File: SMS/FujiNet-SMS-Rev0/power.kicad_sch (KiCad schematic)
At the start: 15 parts, among them Q2 AO3401A, U12 AP63203WU, U13 AP2112K-3.3

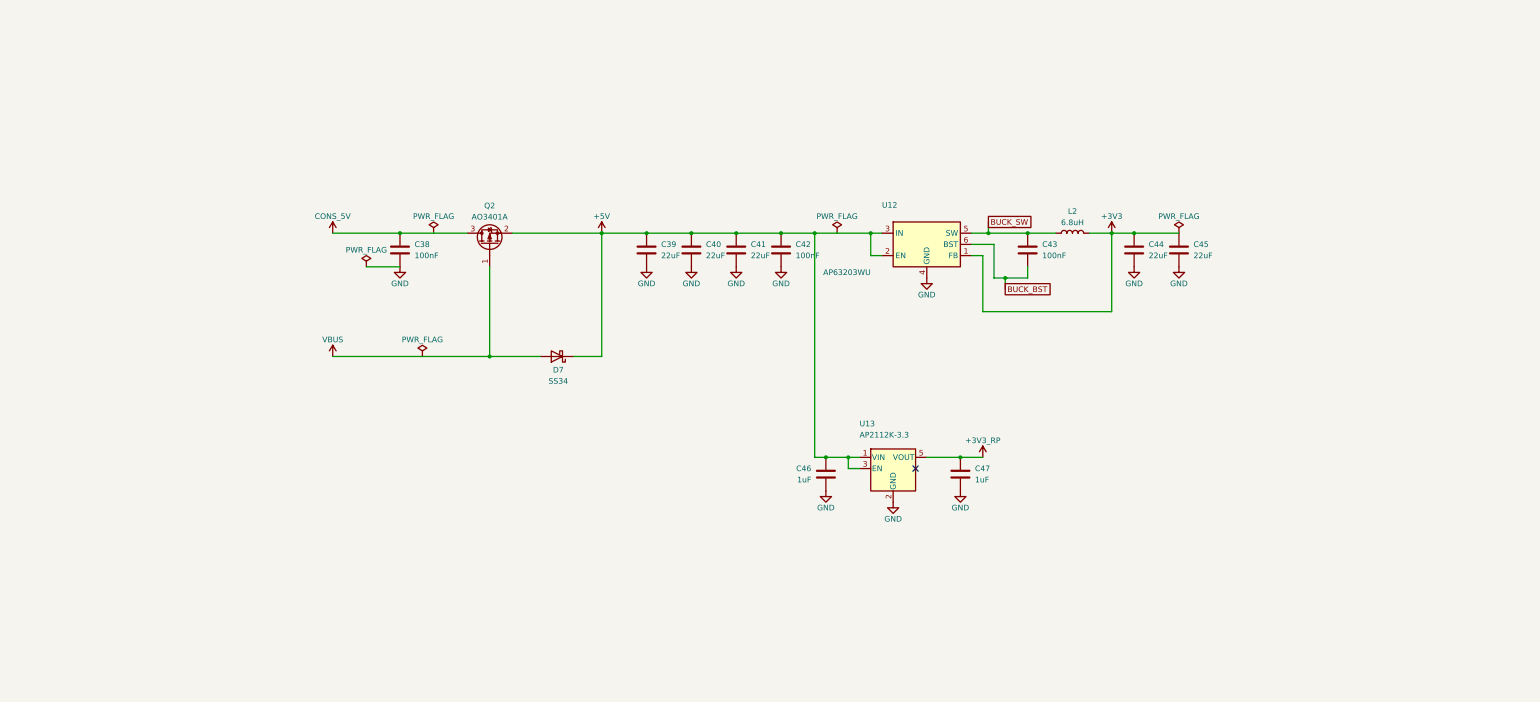
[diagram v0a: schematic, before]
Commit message: SMS Rev0: audit with kicad-happy + datasheets, fix the edge, redraw the schematic
Edge connector: every source (SMS Power slot diagram, little-scale, a 171-5519
scan, raphnet, the barbeque and reidrac footprints) puts the EVEN pins on the
component / label side with pins 1/2 at the right.  The schematic-only
footprint had the faces swapped, which would have put console +5V on /WR.
make_edge_fp.py now writes even pads on F.Cu, odd on B.Cu, 1.75 x 8.75 mm
fingers 0.75-9.5 mm from the edge on a 65.8 mm tab; check_nets.py asserts it
and tools/audit/edge_orientation.py checks it against the sources.

kicad-happy + datasheet audit (docs/design-review-rev0.md Part 1, 27 deep
review findings, gate 27/27): R_VBPD 4.7k VBUS pull-down (SS34 leakage lifts
the P-FET gate), /WAIT gate pull-up 10k -> 4.7k (GPIO34's reset pull-down vs
the 2N7002's 2.5 V threshold), 10 uF bulk on the console 5V.

Schematic: hierarchical sheets wired on a root block diagram (edge -> RP2354B
-> ESP32-S3 -> USB, glue and SRAM under the RP, power below); every sheet
drawn left to right, the glue as a wired logic network by gate depth, the
RP2354B mirrored so its bus faces the console, small sheets on A4.  Parts
are addressed by key (design.py), no more NES reference aliasing.  sch_draw
gains hierarchical labels, sheet blocks, a bus graph and flag / power-pin
lints; gen_sch checks the hierarchy against design.py and names nets by
their last path element (one bus vector per bus: KiCad joins differing
vectors by position).  ERC 0, check_nets 437/437, check_glue 8192/8192.

JLC CPL rotations measured against the EasyEDA footprint of every LCSC part
(tools/audit/jlc); the AS6C4008 has no EasyEDA footprint.

Co-Authored-By: Claude Opus 5.5 <noreply@anthropic.com>
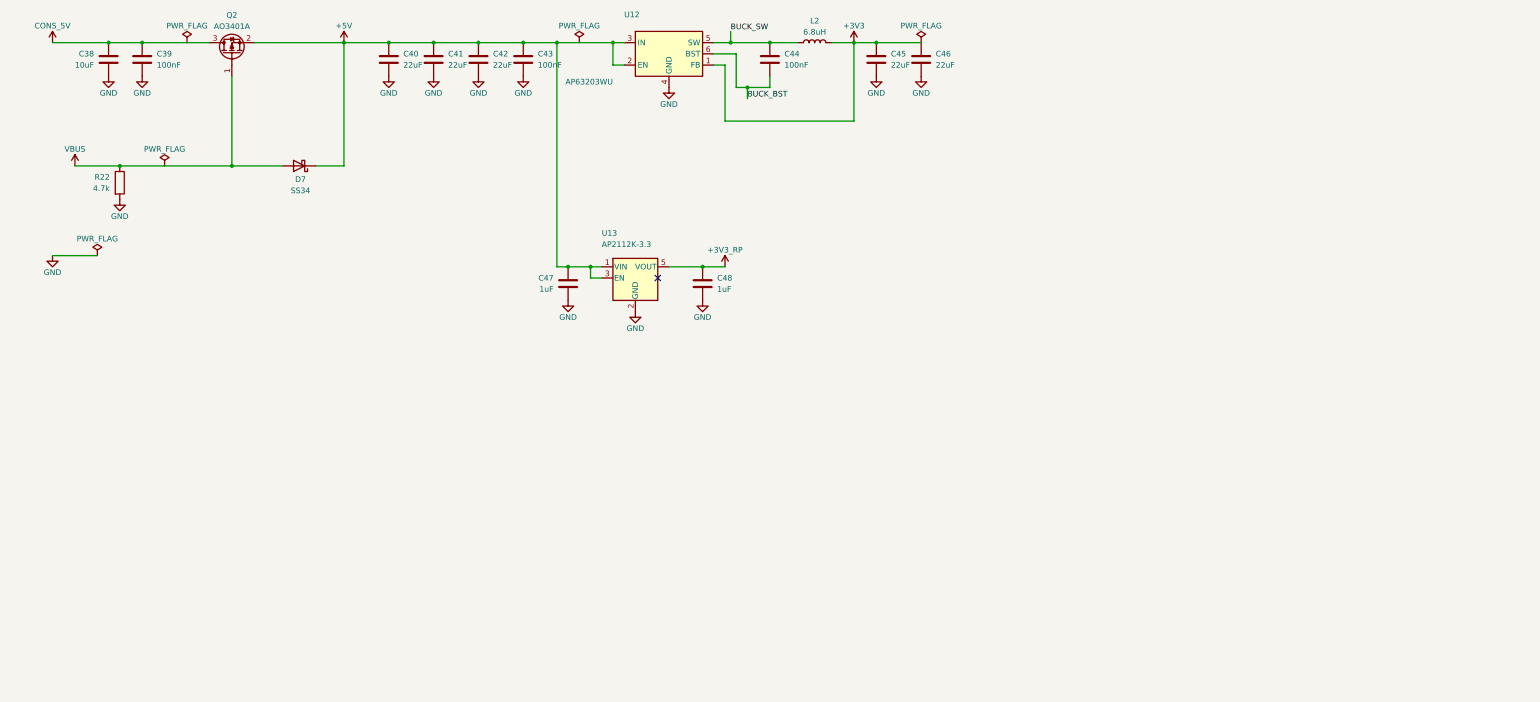
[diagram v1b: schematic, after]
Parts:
- added C48: 1uF, FujiNet-SMS:C_0603_1608Metric, symbol Device:C
- added R22: 4.7k, FujiNet-SMS:R_0603_1608Metric, symbol Device:R
- C38: value 100nF -> 10uF; LCSC C14663 -> C19702; MPN CC0603KRX7R9BB104 -> CL10A106KP8NNNC
- C39, C44: value 22uF -> 100nF; footprint FujiNet-SMS:C_0805_2012Metric -> FujiNet-SMS:C_0603_1608Metric; LCSC C45783 -> C14663; MPN CL21A226MAQNNNE -> CC0603KRX7R9BB104
- C42: value 100nF -> 22uF; footprint FujiNet-SMS:C_0603_1608Metric -> FujiNet-SMS:C_0805_2012Metric; LCSC C14663 -> C45783; MPN CC0603KRX7R9BB104 -> CL21A226MAQNNNE
- C46: value 1uF -> 22uF; footprint FujiNet-SMS:C_0603_1608Metric -> FujiNet-SMS:C_0805_2012Metric; LCSC C15849 -> C45783; MPN CL10A105KB8NNNC -> CL21A226MAQNNNE
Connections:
- net +3V3: now also C46.1; no longer C44.1
- net +3V3_RP: now also C48.1; no longer C47.1
- net +5V: now also C43.1, C47.1; no longer C39.1, C46.1
- net BUCK_BST: now also C44.2; no longer C43.2
- net BUCK_SW: now also C44.1; no longer C43.1
- net CONS_5V: now also C39.1
- net GND: now also C43.2, C48.2, R22.2; no longer C44.2
- net VBUS: now also R22.1
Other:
- moved on the sheet: C38, C39, C40, C41, C42, C43, C44, C45, C46, C47, D7, L2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

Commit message: SMS Rev0 v2: port the FujiNet-7800 tooling, swap the near-stock-out parts
- export.py: JLCPCB and PCBWay packages (PCBWay turnkey BOM, centroid,
  assembly drawing); Manufacturer on every BOM part (design.MFR), written
  to symbols and footprints alike
- edge_geom.py: the SMS edge constants in one place (make_edge_fp,
  gen_pcb, check_gerbers); gen_pcb's body height, holes and In4 split now
  come from placement.py
- footprint paths from the schematic netlist (gen_pcb.fp_sheet_unit), so
  a part's units can be drawn on several sheets (prototype 2026-10-08:
  kicad-cli files it under the first sheet, parity accepts it)
- check_vias, check_gerbers, make_happy_config, stitch_gnd second ring,
  set_models main(), route_board.sh 12 passes / hybrid, DRC at all
  severities
- TL3342 -> TS-1187A-B-A-B (C318884), WS2812B-2020-V6 -> WS2812C-2020-V1
  (C2976072): ~5 in stock on 2026-10-07

Co-Authored-By: Claude Opus 5.5 <noreply@anthropic.com>
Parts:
- C38, C40, C41, C42, C45, C46, C47, C48: Manufacturer (none) -> Samsung Electro-Mechanics
- C39, C43, C44: Manufacturer (none) -> YAGEO
- D7: Manufacturer (none) -> MDD (Microdiode Semiconductor)
- L2: Manufacturer (none) -> Sunlord
- Q2: Manufacturer (none) -> Alpha & Omega Semiconductor
- R22: Manufacturer (none) -> UNI-ROYAL
- U12, U13: Manufacturer (none) -> Diodes Incorporated
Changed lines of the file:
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@@
+			)
+		)
+		(property "Manufacturer" "Alpha & Omega Semiconductor"
+			(at 88.9 63.5 90)
+			(effects
+				(font
+					(size 1.27 1.27)
+				)
+				(hide yes)
 			)
 		)
@@
 			)
 		)
+		(property "Manufacturer" "Samsung Electro-Mechanics"
+			(at 60.96 64.77 0)
+			(effects
+				(font
+					(size 1.27 1.27)
+				)
+				(hide yes)
+			)
+		)
 		(property "LCSC" "C19702"
 			(at 60.96 64.77 0)
@@
 			)
 		)
+		(property "Manufacturer" "YAGEO"
+			(at 68.58 64.77 0)
+			(effects
+				(font
+					(size 1.27 1.27)
+				)
+				(hide yes)
+			)
+		)
 		(property "LCSC" "C14663"
 			(at 68.58 64.77 0)
@@
 			)
 		)
+		(property "Manufacturer" "MDD (Microdiode Semiconductor)"
+			(at 104.14 88.9 0)
+			(effects
+				(font
+					(size 1.27 1.27)
+				)
+				(hide yes)
+			)
+		)
 		(property "LCSC" "C8678"
 			(at 104.14 88.9 0)
@@
 			)
 		)
+		(property "Manufacturer" "UNI-ROYAL"
+			(at 63.5 92.71 0)
+			(effects
+				(font
+					(size 1.27 1.27)
+				)
+				(hide yes)
+			)
+		)
 		(property "LCSC" "C23162"
 			(at 63.5 92.71 0)
@@
 			)
 		)
+		(property "Manufacturer" "Samsung Electro-Mechanics"
+			(at 124.46 64.77 0)
+			(effects
+				(font
+					(size 1.27 1.27)
+				)
+				(hide yes)
+			)
+		)
 		(property "LCSC" "C45783"
 			(at 124.46 64.77 0)
@@
 			)
 		)
+		(property "Manufacturer" "Samsung Electro-Mechanics"
+			(at 134.62 64.77 0)
+			(effects
+				(font
+					(size 1.27 1.27)
+				)
+				(hide yes)
+			)
+		)
 		(property "LCSC" "C45783"
 			(at 134.62 64.77 0)
@@
 			)
 		)
+		(property "Manufacturer" "Samsung Electro-Mechanics"
+			(at 144.78 64.77 0)
+			(effects
+				(font
+					(size 1.27 1.27)
+				)
+				(hide yes)
+			)
+		)
 		(property "LCSC" "C45783"
 			(at 144.78 64.77 0)
@@
 			)
 		)
+		(property "Manufacturer" "YAGEO"
+			(at 154.94 64.77 0)
+			(effects
+				(font
+					(size 1.27 1.27)
+				)
+				(hide yes)
+			)
+		)
 		(property "LCSC" "C14663"
 			(at 154.94 64.77 0)
@@
 			)
 		)
+		(property "Manufacturer" "Diodes Incorporated"
+			(at 187.96 63.5 0)
+			(effects
+				(font
+					(size 1.27 1.27)
+				)
+				(hide yes)
+			)
+		)
 		(property "LCSC" "C780769"
 			(at 187.96 63.5 0)
@@
 			)
 		)
+		(property "Manufacturer" "YAGEO"
+			(at 210.82 64.77 0)
+			(effects
+				(font
+					(size 1.27 1.27)
+				)
+				(hide yes)
+			)
+		)
 		(property "LCSC" "C14663"
 			(at 210.82 64.77 0)
@@
 			)
 		)
+		(property "Manufacturer" "Sunlord"
+			(at 220.98 60.96 90)
+			(effects
+				(font
+					(size 1.27 1.27)
+				)
+				(hide yes)
+			)
+		)
 		(property "LCSC" "C62684"
 			(at 220.98 60.96 90)
@@
 			)
 		)
+		(property "Manufacturer" "Samsung Electro-Mechanics"
+			(at 234.95 64.77 0)
+			(effects
+				(font
+					(size 1.27 1.27)
+				)
+				(hide yes)
+			)
+		)
 		(property "LCSC" "C45783"
 			(at 234.95 64.77 0)
@@
 			)
 		)
+		(property "Manufacturer" "Samsung Electro-Mechanics"
+			(at 245.11 64.77 0)
+			(effects
+				(font
+					(size 1.27 1.27)
+				)
+				(hide yes)
+			)
+		)
 		(property "LCSC" "C45783"
 			(at 245.11 64.77 0)
@@
 			)
 		)
+		(property "Manufacturer" "Diodes Incorporated"
+			(at 180.34 114.3 0)
+			(effects
+				(font
+					(size 1.27 1.27)
+				)
+				(hide yes)
+			)
+		)
 		(property "LCSC" "C51118"
 			(at 180.34 114.3 0)
@@
 			)
 		)
+		(property "Manufacturer" "Samsung Electro-Mechanics"
+			(at 165.1 115.57 0)
+			(effects
+				(font
+					(size 1.27 1.27)
+				)
+				(hide yes)
+			)
+		)
 		(property "LCSC" "C15849"
 			(at 165.1 115.57 0)
@@
 			(at 195.58 115.57 0)
 			(effects
+				(font
+					(size 1.27 1.27)
+				)
+				(hide yes)
+			)
+		)
+		(property "Manufacturer" "Samsung Electro-Mechanics"
+			(at 195.58 115.57 0)
+			(effects

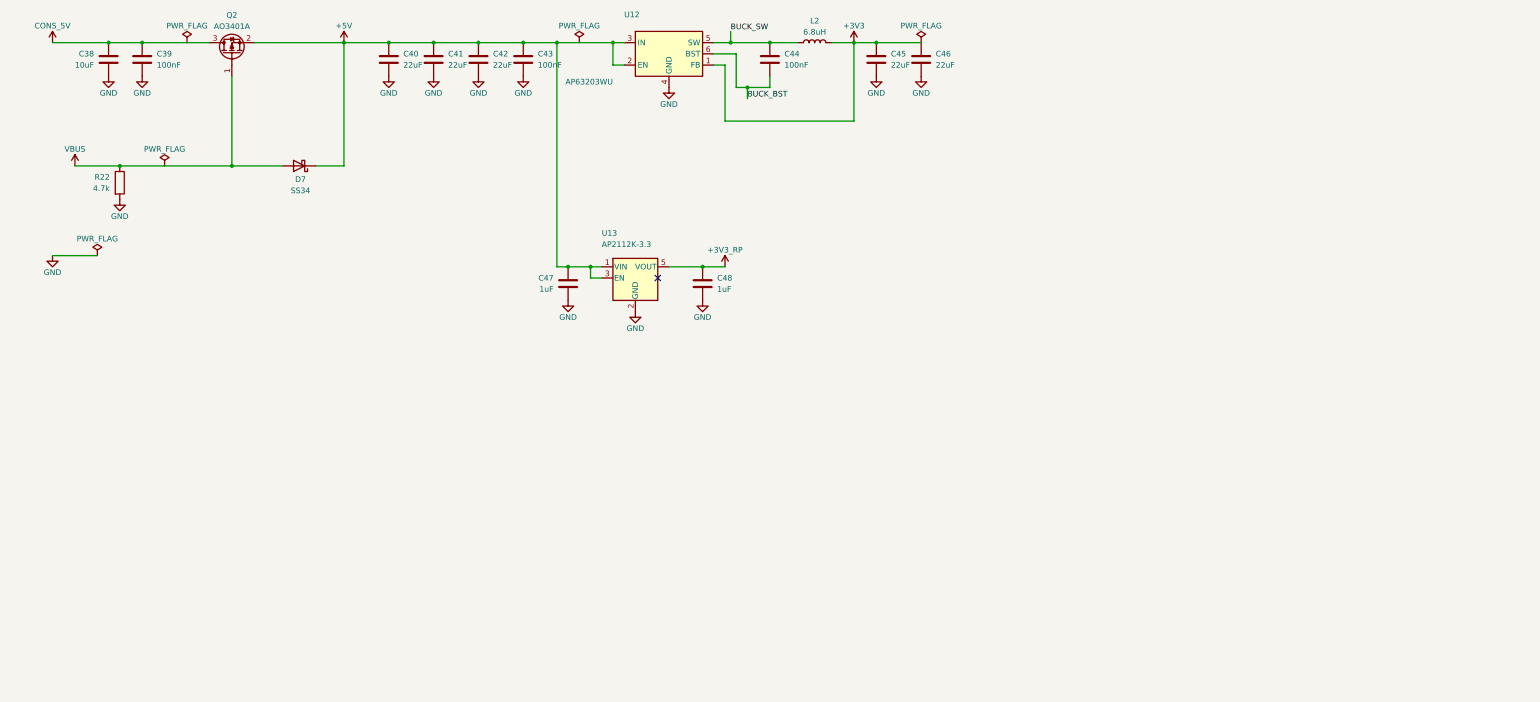
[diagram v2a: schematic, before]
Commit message: SMS Rev0 v2: co-designed floorplan, region sheets, E9 pull-downs, frozen refs and nets
Floorplan study (docs/floorplan-study.md): the SMS edge is the JEDEC
32-pin memory pinout unrolled, so SRAM0 standing upright in the ROM spot
takes A0-A12 / D0-D7 / GND with no crossing.  gen_pcb.sram0_fanin draws
that fan-in locked (funnel, two corner wraps, B-finger jog vias, escape
vias for CE# and OE#).  Four candidates scored and trial-routed in
parallel; P3 (RP2354B straight north of SRAM0, SRAM1 west, glue east over
the strobes) routes best (45 unrouted after 4 passes vs 50 for the first
layout) and reads straight across on the schematic page.

- placement.py: candidates as blocks; the RP2354B + ring as a rigid macro
  (turns as a whole, dvdd_island turns with it); per-variant In4 +5V
  island polygon; label area for the shell
- design.py: sheets are board regions (cart-bus, rp-core, fujinet, usb,
  power); the RP2354B as a two-unit symbol (GPIO on cart-bus, core on
  rp-core); resistor packs one unit per resistor; RP2350-E9 4.7k
  pull-downs on GAME/LOAD/RAM_WE/MBOX/SA19 (check_nets asserts <= 8.2k);
  bring-up pads (CE, OE, WE, PWR_OK, rails, DVDD)
- geographic references (tools/annotate.py -> tools/refs.lock); net names
  frozen in tools/nets.lock (gen_sch fails if a redraw changes one)
- sch_draft.py: an every-pin-labelled draft of the final hierarchy so the
  board is built while the sheets are drawn; sch_draw lint for wired
  sheets (one piece per net, no 4-way junctions, wires clear of text,
  crossing count); sch_place.py mirror check
- check_parts_inside: footprint keep-outs (the S3 antenna bars parts)
- shell: RESET plunger redesigned (captive flange under the guide, stem
  on the TS-1187A actuator, travel asserts, interference part)

ERC 0, parity 126/126, check_nets 442/442, check_glue 8192/8192.
Board placed, not routed yet.

Co-Authored-By: Claude Opus 5.5 <noreply@anthropic.com>
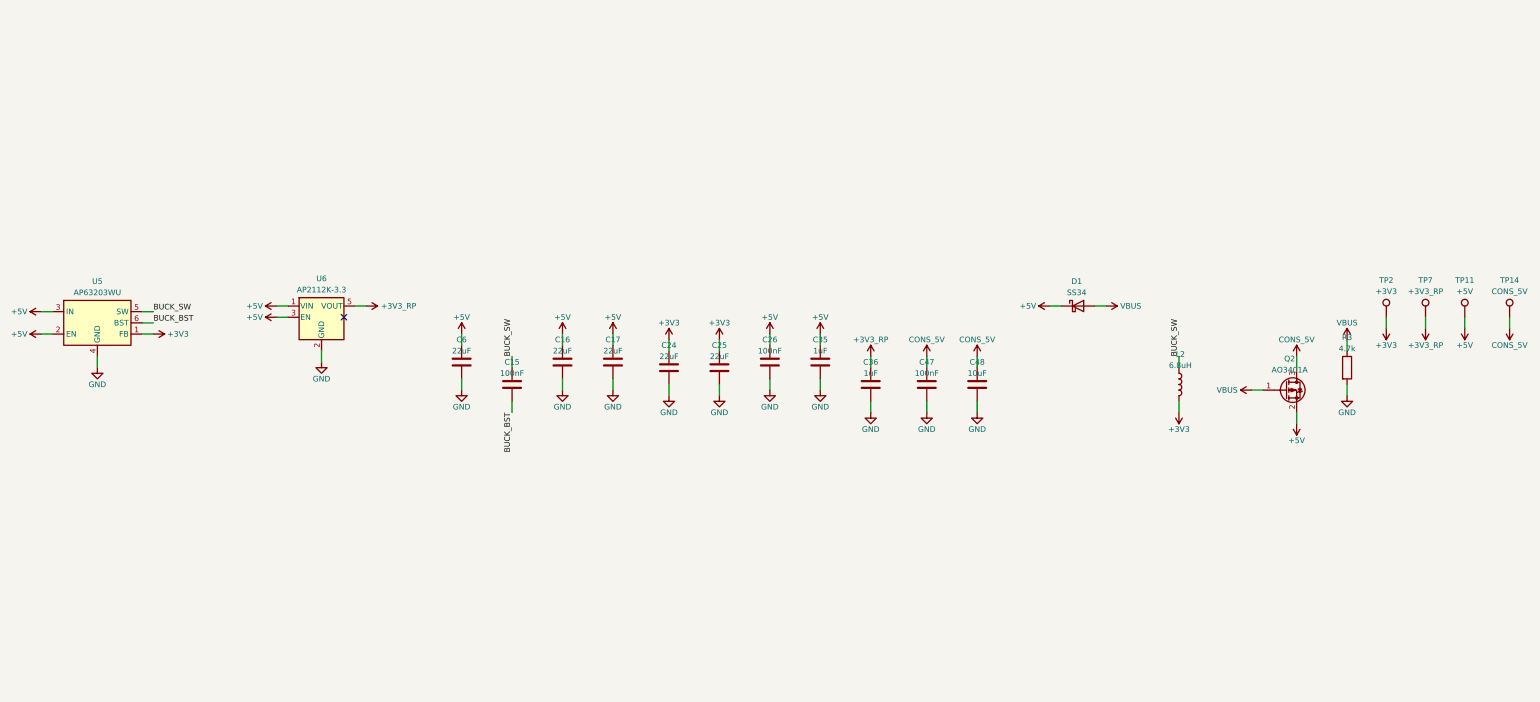
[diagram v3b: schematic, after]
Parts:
- removed C38: 10uF, FujiNet-SMS:C_0603_1608Metric, symbol Device:C
- removed C39, C43, C44: 100nF, FujiNet-SMS:C_0603_1608Metric, symbol Device:C
- removed C40, C41, C42, C45, C46: 22uF, FujiNet-SMS:C_0805_2012Metric, symbol Device:C
- removed D7: SS34, FujiNet-SMS:D_SMA, symbol Diode:SS34
- removed R22: 4.7k, FujiNet-SMS:R_0603_1608Metric, symbol Device:R
- removed U12: AP63203WU, FujiNet-SMS:TSOT-23-6, symbol Regulator_Switching:AP63203WU
- removed U13: AP2112K-3.3, FujiNet-SMS:SOT-23-5, symbol Regulator_Linear:AP2112K-3.3
- added C15, C26: 100nF, FujiNet-SMS:C_0603_1608Metric, symbol Device:C
- added C16, C17, C24, C25, C6: 22uF, FujiNet-SMS:C_0805_2012Metric, symbol Device:C
- added C35, C36: 1uF, FujiNet-SMS:C_0603_1608Metric, symbol Device:C
- added D1: SS34, FujiNet-SMS:D_SMA, symbol Diode:SS34
- added R3: 4.7k, FujiNet-SMS:R_0603_1608Metric, symbol Device:R
- added TP11: +5V, FujiNet-SMS:TestPoint_Pad_D1.5mm, symbol Connector:TestPoint
- added TP14: CONS_5V, FujiNet-SMS:TestPoint_Pad_D1.5mm, symbol Connector:TestPoint
- added TP2: +3V3, FujiNet-SMS:TestPoint_Pad_D1.5mm, symbol Connector:TestPoint
- added TP7: +3V3_RP, FujiNet-SMS:TestPoint_Pad_D1.5mm, symbol Connector:TestPoint
- added U5: AP63203WU, FujiNet-SMS:TSOT-23-6, symbol Regulator_Switching:AP63203WU
- added U6: AP2112K-3.3, FujiNet-SMS:SOT-23-5, symbol Regulator_Linear:AP2112K-3.3
- C47: value 1uF -> 100nF; LCSC C15849 -> C14663; MPN CL10A105KB8NNNC -> CC0603KRX7R9BB104; Manufacturer Samsung Electro-Mechanics -> YAGEO
- C48: value 1uF -> 10uF; LCSC C15849 -> C19702; MPN CL10A105KB8NNNC -> CL10A106KP8NNNC
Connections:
- net +3V3: now also C24.1, C25.1, TP2.1, U5.1 (FB)
- net +3V3_RP: now also C36.1, TP7.1, U6.5 (VOUT); no longer C48.1
- net +5V: now also C16.1, C17.1, C26.1, C35.1, C6.1, D1.1 (K), TP11.1, U5.2 (EN), U5.3 (IN), U6.1 (VIN), U6.3 (EN); no longer C47.1
- net BUCK_BST: now also C15.2, U5.6 (BST)
- net BUCK_SW: now also C15.1, U5.5 (SW)
- net CONS_5V: now also C47.1, C48.1, TP14.1
- net GND: now also C16.2, C17.2, C24.2, C25.2, C26.2, C35.2, C36.2, C6.2, R3.2, U5.4 (GND), U6.2 (GND)
- net VBUS: now also D1.2 (A), R3.1
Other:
- title: FujiNet SMS Rev0 - Power: 5V OR, 3.3V buck, RP LDO -> FujiNet SMS Rev0 - Power: console 5V / USB OR, 3.3V buck, RP LDO
- moved on the sheet: C47, C48, L2, Q2
